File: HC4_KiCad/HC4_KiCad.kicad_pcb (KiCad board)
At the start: 2 copper layers, 150 x 150 mm, 155 parts, among them IC1 RAM, IC10 74HC4002, IC11 74HC161, IC12 74HC377, IC13 74HC161, IC14 74HC161, IC15 74HC161, IC16 74HC257, IC17 74HC257, IC18 74HC00, IC19 74HC32, IC2 ROM, IC20 74HC74, IC21 74HC4053, IC22 74HC04, IC23 74HC151, IC24 74HC14, IC3 74HC153, IC4 74HC153, IC5 74HC153, IC6 74HC153, IC7 74HC283, IC8 74HC244, IC8 74HC257, IC9 74HC244, J1 Power, J2 CE, J3 Expantion_Connector, SW1 SW_SPDT, SW2 Bus_Open, SW3 SW_Push, SW4 SW_Push, SW5 SW_SPDT

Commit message: ICを再配置
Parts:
- moved C1 206.4 mm to (-6.40, 252.9)
- moved J1 206.4 mm to (-7.64, 215.3)
- moved J2 206.4 mm to (-10.8, 254.2)
- moved LD1 206.4 mm to (-21.4, 254.2)
- moved LD2 206.4 mm to (-6.44, 244.0)
- moved LD3 206.4 mm to (-6.44, 247.8)
- moved R1 206.4 mm to (-11.6, 232.0)
- moved R3 206.4 mm to (-11.6, 240.1)
- moved D1 206.4 mm to (-33.8, 256.5)
- moved F1 206.4 mm to (-32.1, 252.1)
- moved IC2 206.4 mm to (-31.9, 210.9)
- moved JP1 206.4 mm to (-10.8, 244.5)
- moved R2 206.4 mm to (-11.6, 236.1)
- moved RN1 206.4 mm to (-47.7, 252.6)
- moved SW1 206.4 mm to (-44.2, 256.8)
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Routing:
- net GND: track 563.8 -> 320.9 mm
- net VCC: track 505.8 -> 290.3 mm

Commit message: 再配置ほぼ完了
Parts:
- removed the CP15 at (102.9, 34.2)
- removed the IC18 at (105.4, 39.2)
- added CP17: 0.1u, Capacitor_THT:C_Disc_D3.0mm_W1.6mm_P2.50mm, F.Cu at (293.4, 190.5)
- added IC20: 74HC00, Package_DIP:DIP-14_W7.62mm_Socket, F.Cu at (293.9, 201.8)
- C4: footprint Capacitor_THT:CP_Radial_D5.0mm_P2.50mm -> Capacitor_THT:C_Radial_D5.0mm_H5.0mm_P2.00mm
- moved IC2 261.6 mm to (217.2, 130.8)
- moved IC13 226.2 mm to (215.9, 69.8)
- moved RN1 222.3 mm to (123.2, 110.5), turned to -90 degrees
- moved RN4 209.0 mm to (229.9, 94.0), turned to 180 degrees
- moved LD10 203.6 mm to (219.7, 88.9), turned to -90 degrees
- moved LD19 199.4 mm to (227.3, 88.9), turned to -90 degrees
- moved LD13 198.5 mm to (222.2, 88.9), turned to -90 degrees
- moved CP12 195.5 mm to (213.4, 49.5), turned to -90 degrees
- moved LD15 193.8 mm to (214.6, 88.9), turned to -90 degrees
- moved LD16 193.3 mm to (224.8, 88.9), turned to -90 degrees
- moved JP1 193.1 mm to (123.2, 105.4), turned to 180 degrees
- moved LD9 192.8 mm to (209.6, 88.9), turned to -90 degrees
- moved SW1 191.6 mm to (99.1, 129.5), turned to 180 degrees
- moved CP13 189.4 mm to (213.4, 64.8), turned to -90 degrees
- moved LD18 188.6 mm to (217.2, 88.9), turned to -90 degrees
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- renumbered CP23 to CP1, CP8 to CP10, CP9 to CP11, CP10 to CP12, CP11 to CP13, CP12 to CP14, CP13 to CP15, CP14 to CP16, CP16 to CP18, CP17 to CP19, CP24 to CP2, CP18 to CP20, CP19 to CP21, CP20 to CP22, CP21 to CP23, CP22 to CP24, CP1 to CP3, CP2 to CP4, CP3 to CP5, CP4 to CP6, CP5 to CP7, CP6 to CP8, CP7 to CP9, IC19 to IC18, IC20 to IC19
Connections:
- net /Address BUS/READ renamed /Instruction Decoder/READ
- net /Address BUS/~{RAM_RD} renamed /Data BUS/~{RD}
- net /Address BUS/~{RAM_WR} renamed /Data BUS/~{WR}
- RN4 pad 2: Net-(LD10-K) -> Net-(LD19-K)
- RN4 pad 3: Net-(LD13-K) -> Net-(LD16-K)
- RN4 pad 4: Net-(LD16-K) -> Net-(LD13-K)
- RN4 pad 5: Net-(LD19-K) -> Net-(LD10-K)
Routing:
- net GND: track 320.9 -> 339.0 mm
- net VCC: track 290.3 -> 273.0 mm
- net Net-(IC1-Q7): track 0.00 -> 8.89 mm
- net Net-(IC1-Q6): track 0.00 -> 8.89 mm
- net Net-(IC1-Q5): track 0.00 -> 8.89 mm
- net Net-(IC1-Q4): track 0.00 -> 8.89 mm
- net (no net): track 8.67 -> 0.00 mm
- net Net-(J2-Pin_1): track 0.00 -> 5.72 mm
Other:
- board size 150 x 150 mm -> 150 x 175 mm
- board text removed: "other"

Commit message: 基板ぬ
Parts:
- removed the D2 at (262.2, 176.4)
- removed the D2 at (262.2, 161.3)
- removed the D3 at (262.2, 180.2)
- removed the D3 at (262.2, 165.1)
- removed the D4 at (262.2, 184.0)
- removed the D4 at (262.2, 168.9)
- removed the D5 at (262.2, 172.7)
- removed the D5 at (261.6, 190.5)
- added D2: D, Library:DO-35_horizontal_anodeup_Smallhole, F.Cu at (152.4, 170.2)
- added D3: D, Library:DO-35_horizontal_anodeup_Smallhole, F.Cu at (152.4, 172.7)
- added D4: D, Library:DO-35_horizontal_anodeup_Smallhole, F.Cu at (152.4, 175.3)
- added D5: D, Library:DO-35_horizontal_anodeup_Smallhole, F.Cu at (152.4, 177.8)
- D10, D11, D12, D13, D14, D15, D16, D17, D18, D19, D20, D21, D22, D23, D24, D25, D26, D27, D28, D29, D30, D31, D32, D33, D34, D35, D36, D37, D38, D39, D40, D41, D6, D7, D8, D9: footprint Diode_THT:D_DO-35_SOD27_P2.54mm_Vertical_AnodeUp -> Library:DO-35_horizontal_anodeup_Smallhole
- moved CP17 229.1 mm to (127.0, 33.0), turned to -90 degrees
- moved LD2 119.4 mm to (233.7, 184.2)
- moved LD3 119.4 mm to (236.2, 184.2)
- moved R2 119.4 mm to (233.7, 188.0)
- moved R3 117.0 mm to (236.2, 188.0)
- moved D7 109.8 mm to (157.5, 172.7)
- moved D8 109.7 mm to (157.5, 175.3)
- moved D9 109.6 mm to (157.5, 177.8)
- moved D6 106.6 mm to (157.5, 170.2)
- moved D16 104.9 mm to (167.6, 175.3)
- moved D17 104.8 mm to (167.6, 177.8)
- moved D13 104.3 mm to (162.6, 177.8)
- moved D12 104.3 mm to (162.6, 175.3)
- moved D11 104.2 mm to (162.6, 172.7)
- moved D10 104.2 mm to (162.6, 170.2)
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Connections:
- net Net-(D11-A) renamed /Instruction Decoder/~{i6}
- net Net-(D12-A) renamed /Instruction Decoder/~{i5}
- net Net-(D13-A) renamed /Instruction Decoder/~{i4}
- net Net-(IC18-Pad4) renamed /Instruction Decoder/~{i7}
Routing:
- net VCC: track 273.0 -> 362.3 mm, vias 7 -> 0
- net /ALU/I3a: track 0.00 -> 64.7 mm, vias 0 -> 1
- net /ALU/I2a: track 0.00 -> 63.8 mm, vias 0 -> 1
- net /ALU/I1a: track 0.57 -> 63.6 mm, vias 0 -> 1
- net /ALU/I0a: track 0.00 -> 61.2 mm
- net /Instruction Decoder/ALU_~{Eb}: track 0.00 -> 28.9 mm
- net GND: track 339.0 -> 362.1 mm, vias 5 -> 1
- net /ALU/Internal_A2: track 0.00 -> 20.9 mm
- net /Data BUS/Stack3: track 10.2 -> 0.00 mm
- net /Data BUS/Stack2: track 10.2 -> 0.00 mm
- net /Data BUS/Stack1: track 10.2 -> 0.00 mm
- net /Data BUS/Stack0: track 10.2 -> 0.00 mm
- net /ALU/Internal_A3: track 0.00 -> 9.76 mm
- net Net-(IC1-Q7): track 8.89 -> 0.00 mm
- net Net-(IC1-Q6): track 8.89 -> 0.00 mm
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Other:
- board text added: "Address Bus"
- board text removed: "Adress Bus"

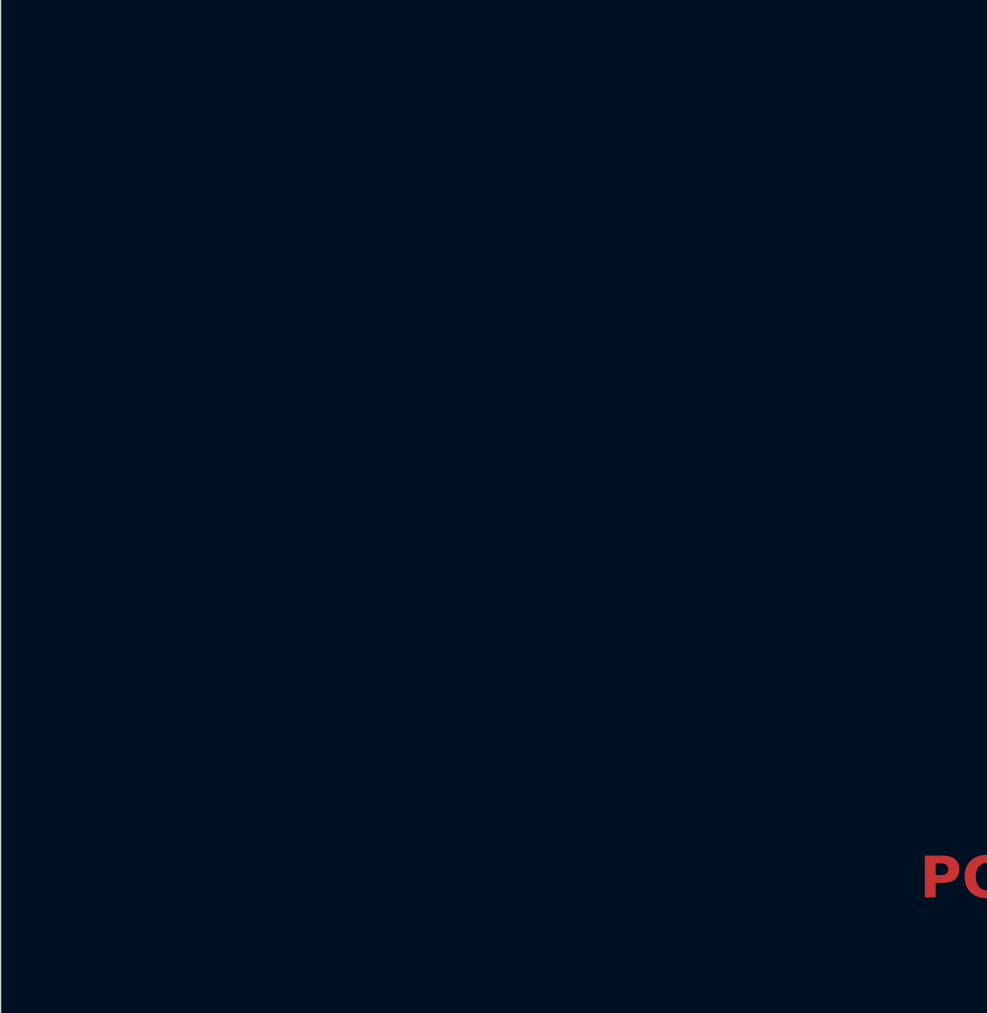
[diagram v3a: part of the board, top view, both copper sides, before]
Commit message: StackLEDつけた
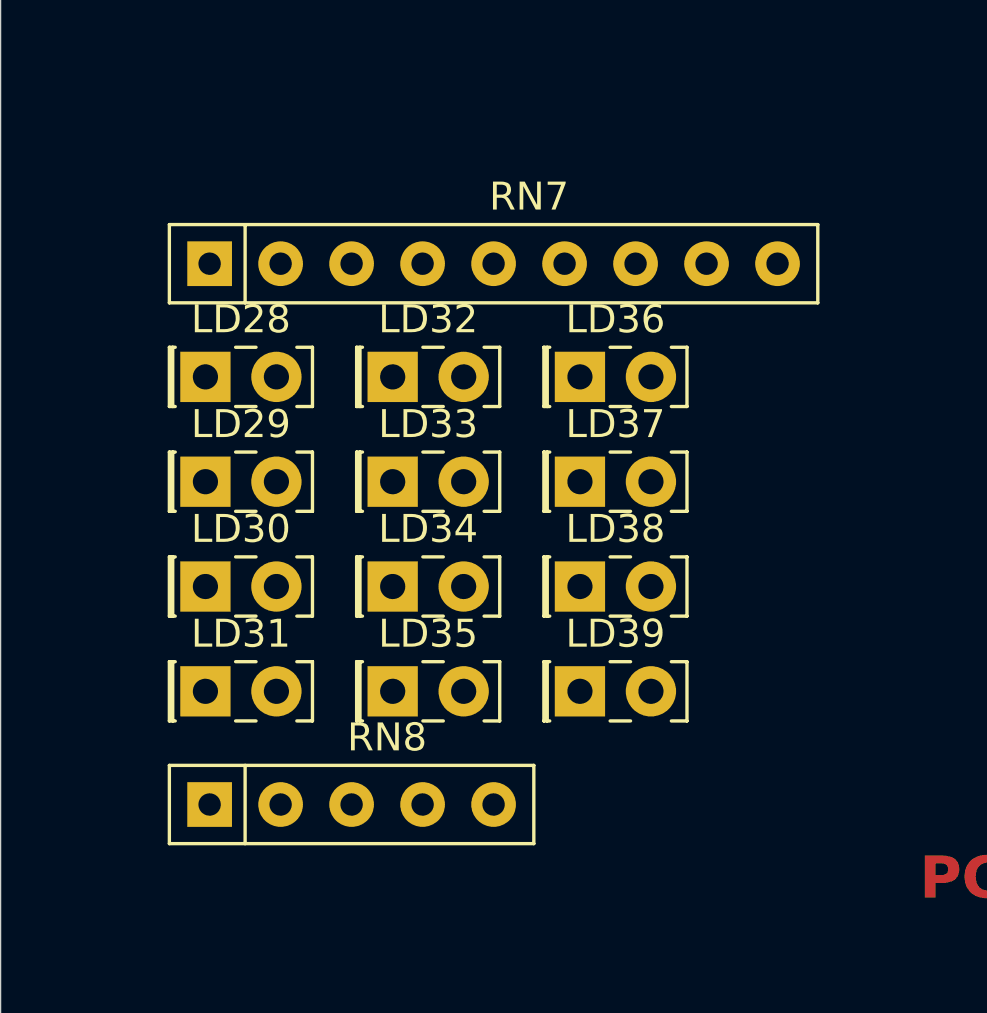
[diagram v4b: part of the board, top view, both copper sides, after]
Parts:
- added LD28: LED, LED_THT:LED_Rectangular_W5.0mm_H2.0mm, F.Cu at (248.8, 44.7)
- added LD29: LED, LED_THT:LED_Rectangular_W5.0mm_H2.0mm, F.Cu at (248.8, 48.4)
- added LD30: LED, LED_THT:LED_Rectangular_W5.0mm_H2.0mm, F.Cu at (248.8, 52.2)
- added LD31: LED, LED_THT:LED_Rectangular_W5.0mm_H2.0mm, F.Cu at (248.8, 55.9)
- added LD32: LED, LED_THT:LED_Rectangular_W5.0mm_H2.0mm, F.Cu at (255.5, 44.7)
- added LD33: LED, LED_THT:LED_Rectangular_W5.0mm_H2.0mm, F.Cu at (255.5, 48.4)
- added LD34: LED, LED_THT:LED_Rectangular_W5.0mm_H2.0mm, F.Cu at (255.5, 52.2)
- added LD35: LED, LED_THT:LED_Rectangular_W5.0mm_H2.0mm, F.Cu at (255.5, 55.9)
- added LD36: LED, LED_THT:LED_Rectangular_W5.0mm_H2.0mm, F.Cu at (262.2, 44.7)
- added LD37: LED, LED_THT:LED_Rectangular_W5.0mm_H2.0mm, F.Cu at (262.2, 48.4)
- added LD38: LED, LED_THT:LED_Rectangular_W5.0mm_H2.0mm, F.Cu at (262.2, 52.2)
- added LD39: LED, LED_THT:LED_Rectangular_W5.0mm_H2.0mm, F.Cu at (262.2, 55.9)
- added RN7: R_Network08_Split, Resistor_THT:R_Array_SIP9, F.Cu at (248.9, 40.6)
- added RN8: R_Network04_Split, Resistor_THT:R_Array_SIP5, F.Cu at (248.9, 60.0)

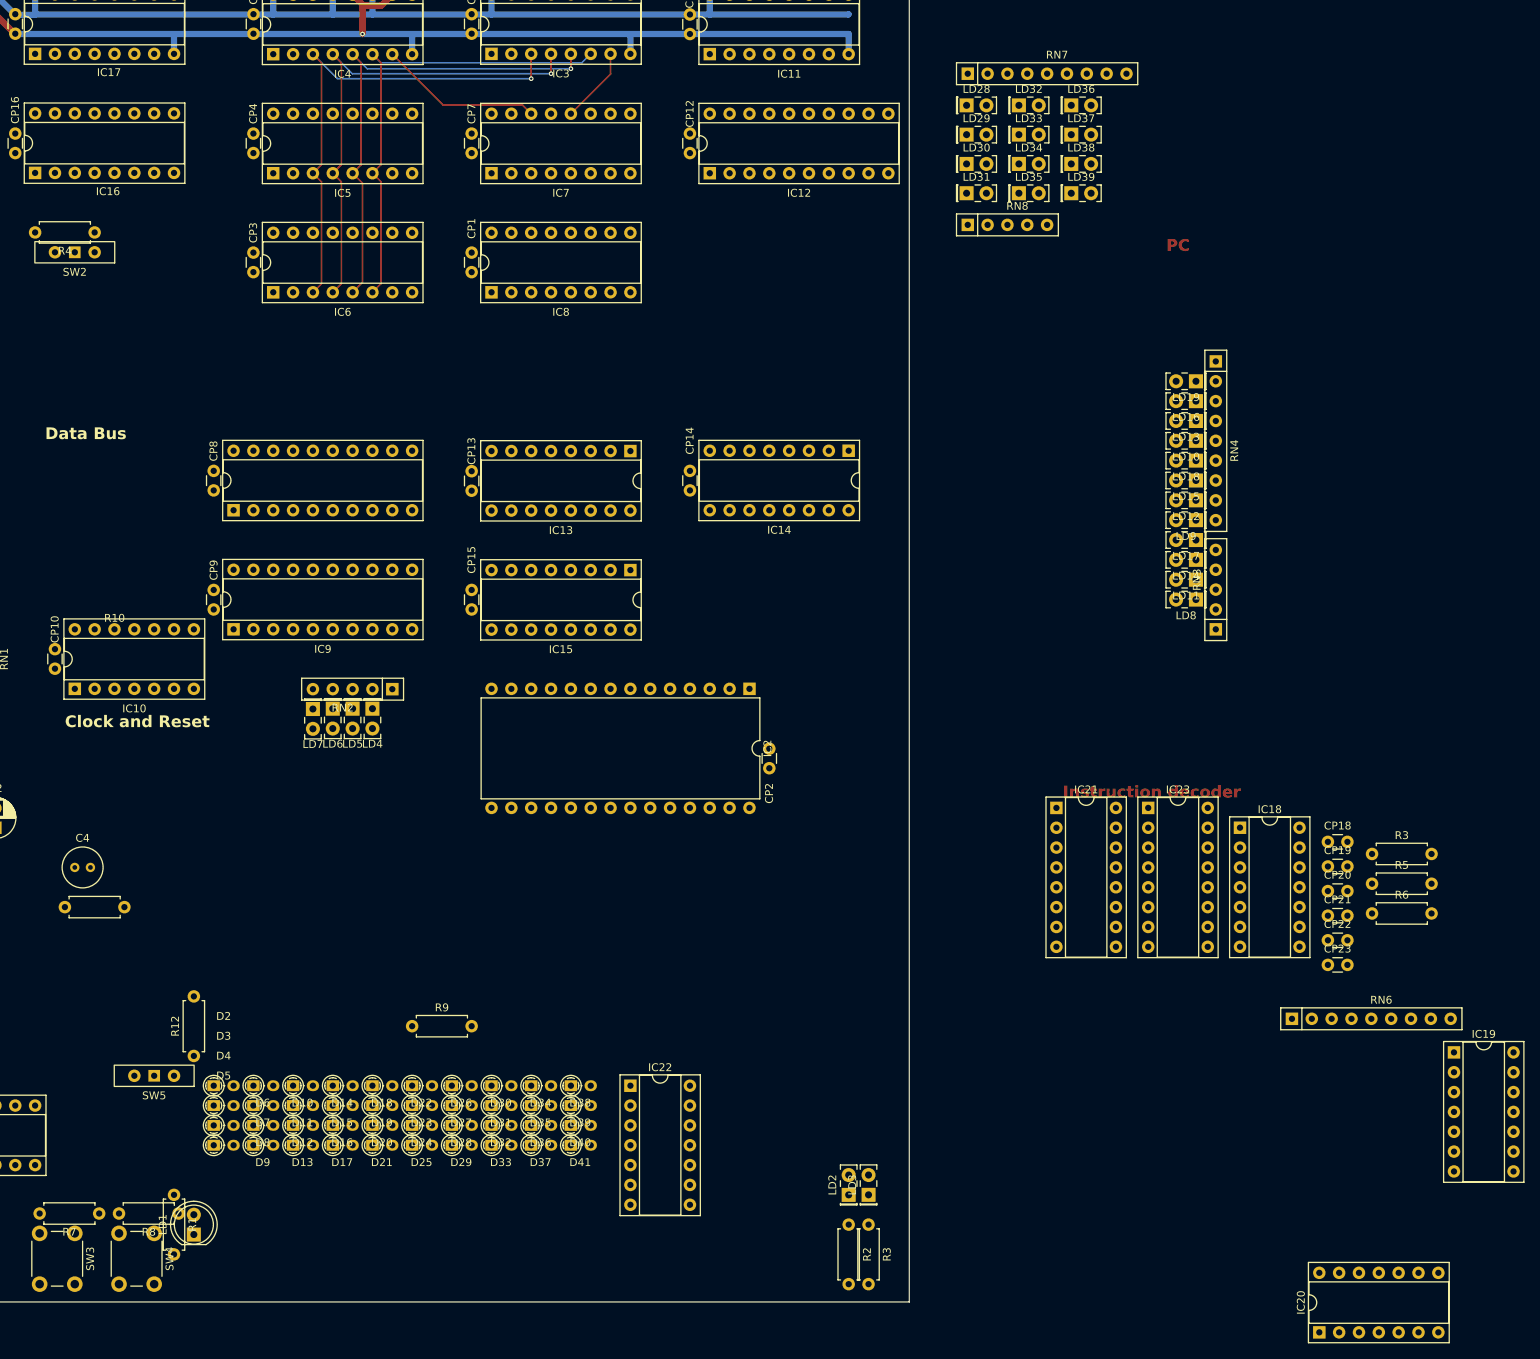
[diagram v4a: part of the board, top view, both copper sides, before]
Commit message: とりあえずIC配置確定
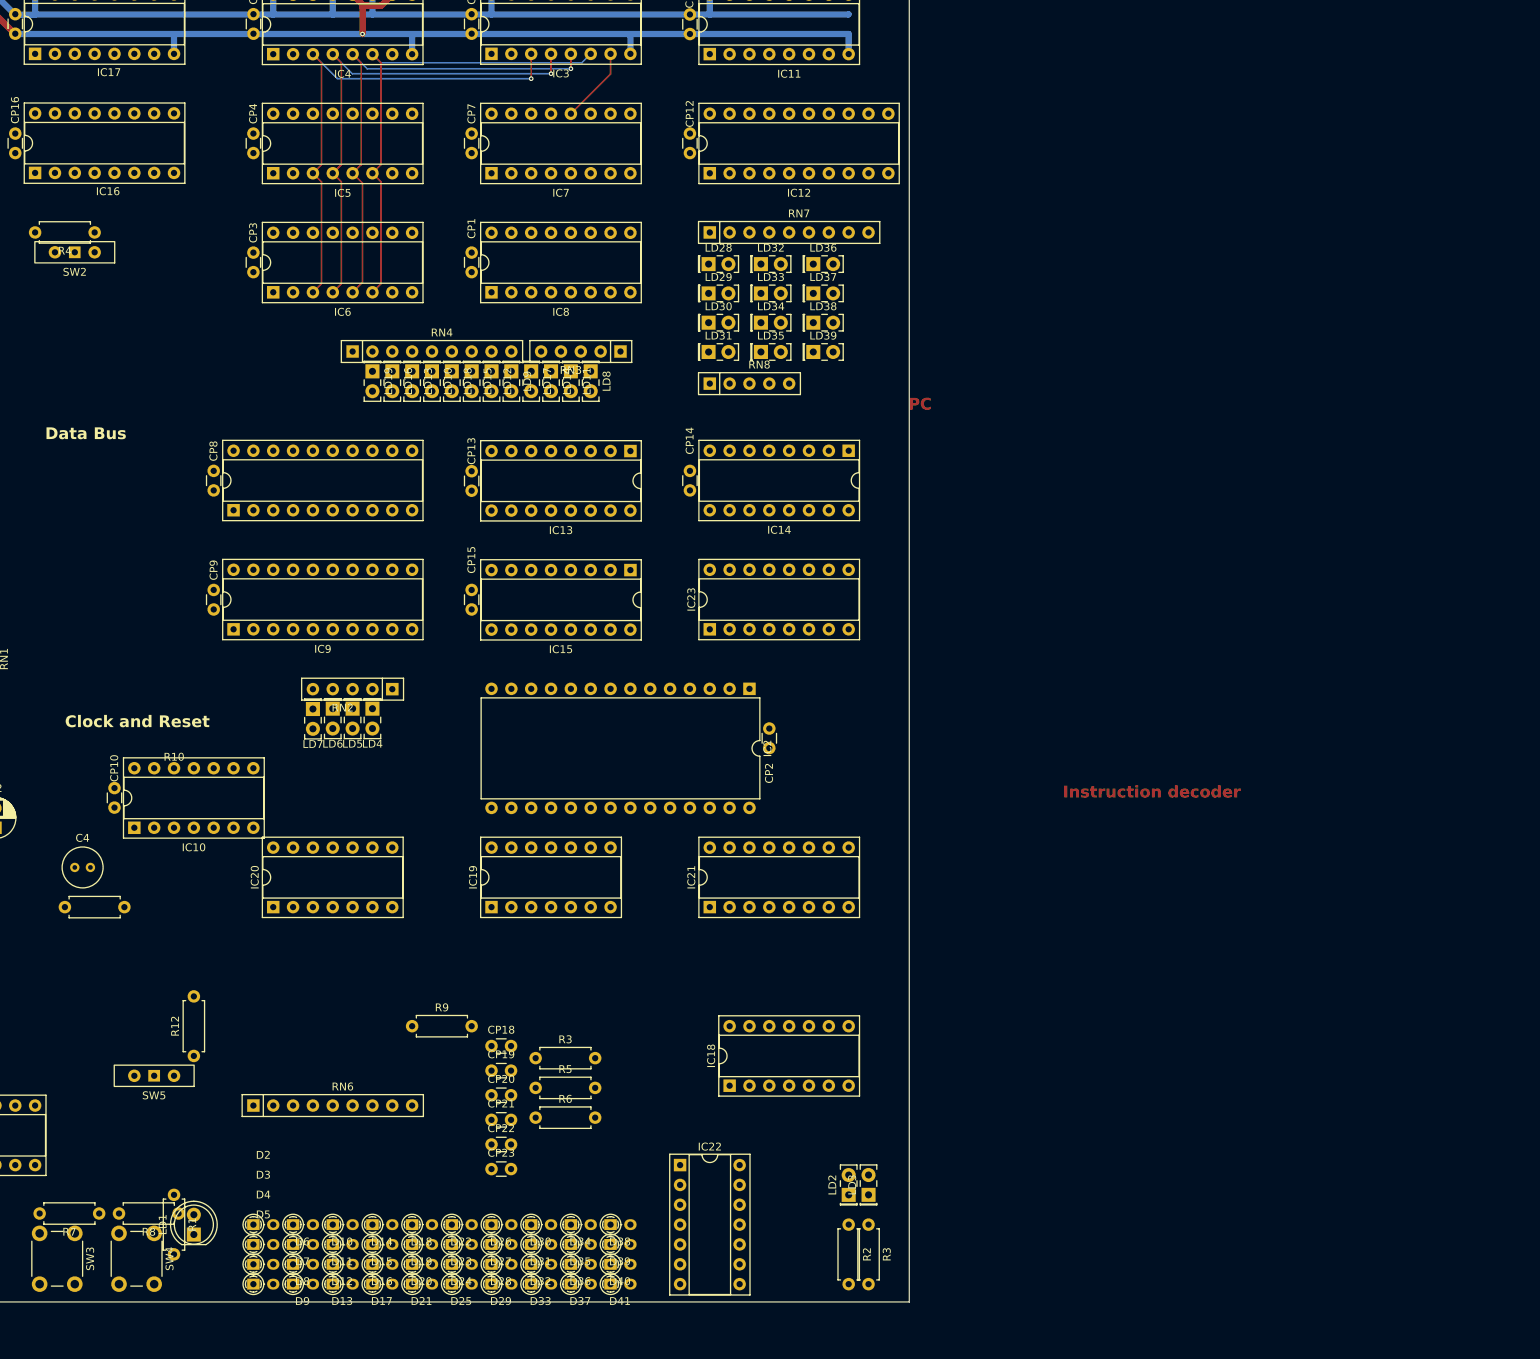
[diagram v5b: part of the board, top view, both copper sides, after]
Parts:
- moved IC20 144.5 mm to (160.0, 147.3)
- moved RN6 133.4 mm to (157.5, 172.7)
- moved IC19 124.6 mm to (188.0, 147.3), turned to 90 degrees
- moved RN4 110.5 mm to (170.2, 76.2), turned to 0 degrees
- moved R3 110.2 mm to (193.6, 166.7)
- moved R5 110.2 mm to (193.6, 170.5)
- moved R6 110.2 mm to (193.6, 174.3)
- moved CP20 110.2 mm to (188.0, 171.4)
- moved CP21 110.2 mm to (188.0, 174.6)
- moved CP18 110.2 mm to (188.0, 165.1)
- moved CP19 110.2 mm to (188.0, 168.2)
- moved CP22 110.2 mm to (188.0, 177.7)
- moved CP23 110.2 mm to (188.0, 180.8)
- moved LD19 105.4 mm to (172.7, 78.7), turned to -90 degrees
- moved LD16 102.9 mm to (175.3, 78.7), turned to -90 degrees
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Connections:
- IC10 pad 1: /Data BUS/BUS_Zero -> /ALU/I1a
- IC10 pad 10: Net-(D18-K) -> /Data BUS/Stack2
- IC10 pad 11: Net-(D22-K) -> /Data BUS/Stack1
- IC10 pad 12: Net-(D22-K) -> /Data BUS/Stack0
- IC10 pad 13: /ALU/I1a -> /Data BUS/BUS_Zero
- IC10 pad 2: /Data BUS/Stack0 -> Net-(D18-K)
- IC10 pad 3: /Data BUS/Stack1 -> Net-(D18-K)
- IC10 pad 4: /Data BUS/Stack2 -> Net-(D22-K)
- IC10 pad 5: /Data BUS/Stack3 -> Net-(D22-K)
- IC10 pad 9: Net-(D18-K) -> /Data BUS/Stack3
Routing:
- net /ALU/Internal_A2: track 20.9 -> 0.00 mm

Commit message: 電源配線ほぼ完了
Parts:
- removed the IC8 at (154.9, 96.5)
- moved CP23 78.4 mm to (213.4, 106.7), turned to -90 degrees
- moved CP1 74.4 mm to (111.8, 53.3), turned to 180 degrees
- moved CP8 43.3 mm to (185.4, 63.5)
- moved CP20 42.2 mm to (157.5, 142.3), turned to -90 degrees
- moved CP21 41.1 mm to (213.4, 142.2), turned to -90 degrees
- moved CP22 30.4 mm to (218.4, 177.8), turned to 180 degrees
- moved CP18 27.9 mm to (215.9, 165.1), turned to -90 degrees
- moved CP19 26.1 mm to (185.4, 142.3), turned to -90 degrees
- moved LD39 26.1 mm to (203.2, 78.7), turned to -90 degrees
- moved LD38 24.2 mm to (205.7, 78.7), turned to -90 degrees
- moved RN7 23.4 mm to (233.7, 76.2), turned to 180 degrees
- moved LD37 23.1 mm to (208.3, 78.7), turned to -90 degrees
- moved LD36 22.9 mm to (210.8, 78.7), turned to -90 degrees
- moved LD28 20.6 mm to (231.1, 78.7), turned to -90 degrees
- moved LD29 16.3 mm to (228.6, 78.7), turned to -90 degrees
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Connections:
- RN7 pad 1: Net-(LD28-K) -> GND
- RN7 pad 2: GND -> Net-(LD28-K)
- RN7 pad 3: GND -> Net-(LD29-K)
- RN7 pad 4: GND -> Net-(LD30-K)
- RN7 pad 5: GND -> Net-(LD31-K)
- RN7 pad 6: GND -> Net-(LD32-K)
- RN7 pad 7: GND -> Net-(LD33-K)
- RN7 pad 8: GND -> Net-(LD34-K)
- RN7 pad 9: GND -> Net-(LD35-K)
- RN8 pad 1: Net-(LD36-K) -> GND
- RN8 pad 2: GND -> Net-(LD36-K)
- RN8 pad 3: GND -> Net-(LD37-K)
- RN8 pad 4: GND -> Net-(LD38-K)
- RN8 pad 5: GND -> Net-(LD39-K)
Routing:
- net GND: track 362.1 -> 1284.7 mm, vias 1 -> 15
- net VCC: track 362.3 -> 1055.9 mm, vias 0 -> 11
